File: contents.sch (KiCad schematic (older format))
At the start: 38 parts

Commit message: power
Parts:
- removed C?: 22u, Discret:C1V8, symbol CP
- removed C?: 1u, Capacitors_SMD:C_1210_HandSoldering, symbol C
- removed C?: 0,47u, Capacitors_SMD:C_1210_HandSoldering, symbol C
- removed U?: 7805, TO_SOT_Packages_THT:TO-220_Neutral123_Horizontal, symbol 7805
- added C?: 470uF, symbol CP
- added C?: 10uF, symbol C
- added C?: 100nF, symbol C
- added D?: D_Schottky, symbol D_Schottky
- added P?: Power jack, Pin_Headers:Pin_Header_Straight_1x02, symbol CONN_01X02
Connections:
- wire segments 83 -> 90
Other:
- moved on the sheet: U?
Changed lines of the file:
@@
-$EndComp
-$Comp
-L +12V #PWR?
-U 1 1 595CD701
-P 2200 5500
-F 0 "#PWR?" H 2200 5350 50  0001 C CNN
-F 1 "+12V" H 2200 5640 50  0000 C CNN
-F 2 "" H 2200 5500 50  0000 C CNN
-F 3 "" H 2200 5500 50  0000 C CNN
-	1    2200 5500
-	0    -1   -1   0
-$EndComp
-$Comp
-L 7805 U?
-U 1 1 595CD702
-P 3000 5550
-F 0 "U?" H 3150 5354 50  0000 C CNN
-F 1 "7805" H 3000 5750 50  0000 C CNN
-F 2 "TO_SOT_Packages_THT:TO-220_Neutral123_Horizontal" H 3000 5550 50  0001 C CNN
-F 3 "" H 3000 5550 50  0000 C CNN
-	1    3000 5550
-	1    0    0    -1
-$EndComp
-$Comp
-L GND #PWR?
-U 1 1 595CD703
-P 3000 6100
-F 0 "#PWR?" H 3000 5850 50  0001 C CNN
-F 1 "GND" H 3000 5950 50  0000 C CNN
-F 2 "" H 3000 6100 50  0000 C CNN
-F 3 "" H 3000 6100 50  0000 C CNN
-	1    3000 6100
-	1    0    0    -1
-$EndComp
-$Comp
-L CP C?
-U 1 1 595CD704
-P 2300 5650
-F 0 "C?" H 2325 5750 50  0000 L CNN
-F 1 "22u" H 2325 5550 50  0000 L CNN
-F 2 "Discret:C1V8" H 2338 5500 50  0001 C CNN
-F 3 "" H 2300 5650 50  0000 C CNN
-	1    2300 5650
-	1    0    0    -1
-$EndComp
-$Comp
-L C C?
-U 1 1 595CD705
-P 2550 5650
-F 0 "C?" H 2575 5750 50  0000 L CNN
-F 1 "1u" H 2575 5550 50  0000 L CNN
-F 2 "Capacitors_SMD:C_1210_HandSoldering" H 2588 5500 50  0001 C CNN
-F 3 "" H 2550 5650 50  0000 C CNN
-	1    2550 5650
-	1    0    0    -1
-$EndComp
-$Comp
-L C C?
-U 1 1 595CD706
-P 3800 5650
-F 0 "C?" H 3825 5750 50  0000 L CNN
-F 1 "0,47u" H 3825 5550 50  0000 L CNN
-F 2 "Capacitors_SMD:C_1210_HandSoldering" H 3838 5500 50  0001 C CNN
-F 3 "" H 3800 5650 50  0000 C CNN
-	1    3800 5650
-	1    0    0    -1
-$EndComp
-$Comp
-L +5V #PWR?
-U 1 1 595CD707
-P 4300 5500
-F 0 "#PWR?" H 4300 5350 50  0001 C CNN
-F 1 "+5V" H 4300 5640 50  0000 C CNN
-F 2 "" H 4300 5500 50  0000 C CNN
-F 3 "" H 4300 5500 50  0000 C CNN
-	1    4300 5500
-	0    1    1    0
-$EndComp
-$Comp
-L GND #PWR?
-U 1 1 595CD708
-P 2450 6100
-F 0 "#PWR?" H 2450 5850 50  0001 C CNN
-F 1 "GND" H 2450 5950 50  0000 C CNN
-F 2 "" H 2450 6100 50  0000 C CNN
-F 3 "" H 2450 6100 50  0000 C CNN
-	1    2450 6100
-	1    0    0    -1
-$EndComp
-$Comp
-L GND #PWR?
-U 1 1 595CD709
-P 3800 6100
-F 0 "#PWR?" H 3800 5850 50  0001 C CNN
-F 1 "GND" H 3800 5950 50  0000 C CNN
-F 2 "" H 3800 6100 50  0000 C CNN
-F 3 "" H 3800 6100 50  0000 C CNN
-	1    3800 6100
-	1    0    0    -1
 $EndComp
 $Comp
@@
 L GND #PWR?
 U 1 1 595CD70B
-P 1500 5800
-F 0 "#PWR?" H 1500 5550 50  0001 C CNN
-F 1 "GND" H 1500 5650 50  0000 C CNN
-F 2 "" H 1500 5800 50  0000 C CNN
-F 3 "" H 1500 5800 50  0000 C CNN
-	1    1500 5800
+P 1500 6100
+F 0 "#PWR?" H 1500 5850 50  0001 C CNN
+F 1 "GND" H 1500 5950 50  0000 C CNN
+F 2 "" H 1500 6100 50  0000 C CNN
+F 3 "" H 1500 6100 50  0000 C CNN
+	1    1500 6100
 	1    0    0    -1
 $EndComp
@@
 Connection ~ 10550 5200
 Wire Wire Line
-	2200 5500 2600 5500
-Connection ~ 2300 5500
-Connection ~ 2550 5500
-Wire Wire Line
-	2300 5800 2550 5800
-Wire Wire Line
-	2450 6100 2450 5800
-Connection ~ 2450 5800
-Wire Wire Line
-	3000 5800 3000 6100
-Wire Wire Line
-	3400 5500 4300 5500
-Connection ~ 3800 5500
-Wire Wire Line
-	3800 5800 3800 6100
-Wire Wire Line
-	1300 5500 1550 5500
+	1300 5500 1750 5500
 Wire Wire Line
 	1300 5600 1500 5600
 Wire Wire Line
-	1500 5600 1500 5800
+	1500 5600 1500 6100
 $Comp
 L POT-RESCUE-Arpette RV?
@@
 Wire Wire Line
 	10550 5550 8500 5550
-Entry Wire Line
-	1200 5500 1300 5600
 Text GLabel 8850 1750 0    60   Input ~ 0
 SSR3
@@
 L TPS54302 U?
 U 1 1 59A7BEB1
-P 3000 4850
-F 0 "U?" H 3000 4650 60  0000 C CNN
-F 1 "TPS54302" H 3000 4850 60  0000 C CNN
-F 2 "" H 3100 4850 60  0001 C CNN
-F 3 "" H 3100 4850 60  0001 C CNN
-	1    3000 4850
-	1    0    0    -1
-$EndComp
+P 4350 5700
+F 0 "U?" H 4350 5500 60  0000 C CNN
+F 1 "TPS54302" H 4350 5700 60  0000 C CNN
+F 2 "" H 4450 5700 60  0001 C CNN
+F 3 "" H 4450 5700 60  0001 C CNN
+	1    4350 5700
+	1    0    0    -1
+$EndComp
+$Comp
+L D_Schottky D?
+U 1 1 59A80FF7
+P 1900 5500
+F 0 "D?" H 1900 5600 50  0000 C CNN
+F 1 "D_Schottky" H 1900 5400 50  0000 C CNN
+F 2 "" H 1900 5500 50  0001 C CNN
+F 3 "" H 1900 5500 50  0001 C CNN
+	1    1900 5500
+	-1   0    0    1
+$EndComp
+$Comp
+L CONN_01X02 P?
+U 1 1 59A81E1F
+P 1100 4950
+F 0 "P?" H 1100 5100 50  0000 C CNN
+F 1 "Power jack" V 1200 4950 50  0000 C CNN
+F 2 "Pin_Headers:Pin_Header_Straight_1x02" H 1100 4950 50  0001 C CNN
+F 3 "" H 1100 4950 50  0000 C CNN
+	1    1100 4950
+	-1   0    0    1
+$EndComp
+$Comp
+L GND #PWR?
+U 1 1 59A81F07
+P 1500 5150
+F 0 "#PWR?" H 1500 4900 50  0001 C CNN
+F 1 "GND" H 1500 5000 50  0000 C CNN
+F 2 "" H 1500 5150 50  0000 C CNN
+F 3 "" H 1500 5150 50  0000 C CNN
+	1    1500 5150
+	1    0    0    -1
+$EndComp
+Wire Wire Line
+	1300 5000 1500 5000
+Wire Wire Line
+	1500 5000 1500 5150
+Wire Wire Line
+	1650 5500 1650 4900
+Wire Wire Line
+	1650 4900 1300 4900
+Connection ~ 1650 5500
+$Comp
+L CP C?
+U 1 1 59A94127
+P 2150 5750
+F 0 "C?" H 2175 5850 50  0000 L CNN
+F 1 "470uF" H 2175 5650 50  0000 L CNN
+F 2 "" H 2188 5600 50  0001 C CNN
+F 3 "" H 2150 5750 50  0001 C CNN
+	1    2150 5750
+	1    0    0    -1
+$EndComp
+$Comp
+L C C?
+U 1 1 59A94628
+P 2450 5750
+F 0 "C?" H 2475 5850 50  0000 L CNN
+F 1 "10uF" H 2475 5650 50  0000 L CNN
+F 2 "" H 2488 5600 50  0001 C CNN
+F 3 "" H 2450 5750 50  0001 C CNN
+	1    2450 5750
+	1    0    0    -1
+$EndComp
+Wire Wire Line
+	2050 5500 3700 5500
+Wire Wire Line
+	2150 5500 2150 5600
+Wire Wire Line
+	2450 5500 2450 5600
+Connection ~ 2150 5500
+Connection ~ 2450 5500
+$Comp
+L C C?
+U 1 1 59A94B39
+P 2800 5750
+F 0 "C?" H 2825 5850 50  0000 L CNN
+F 1 "100nF" H 2825 5650 50  0000 L CNN
+F 2 "" H 2838 5600 50  0001 C CNN
+F 3 "" H 2800 5750 50  0001 C CNN
+	1    2800 5750
+	1    0    0    -1
+$EndComp
+$Comp
+L GND #PWR?
+U 1 1 59A963C8
+P 2150 6100
+F 0 "#PWR?" H 2150 5850 50  0001 C CNN
+F 1 "GND" H 2150 5950 50  0000 C CNN
+F 2 "" H 2150 6100 50  0000 C CNN
+F 3 "" H 2150 6100 50  0000 C CNN
+	1    2150 6100
+	1    0    0    -1
+$EndComp
+$Comp
+L GND #PWR?
+U 1 1 59A96448
+P 2450 6100
+F 0 "#PWR?" H 2450 5850 50  0001 C CNN
+F 1 "GND" H 2450 5950 50  0000 C CNN
+F 2 "" H 2450 6100 50  0000 C CNN
+F 3 "" H 2450 6100 50  0000 C CNN
+	1    2450 6100
+	1    0    0    -1
+$EndComp
+$Comp
+L GND #PWR?
+U 1 1 59A964C8
+P 2800 6100
+F 0 "#PWR?" H 2800 5850 50  0001 C CNN
+F 1 "GND" H 2800 5950 50  0000 C CNN
+F 2 "" H 2800 6100 50  0000 C CNN
+F 3 "" H 2800 6100 50  0000 C CNN
+	1    2800 6100
+	1    0    0    -1
+$EndComp
+Wire Wire Line
+	2150 5900 2150 6100
+Wire Wire Line
+	2450 5900 2450 6100
+Wire Wire Line
+	2800 5900 2800 6100
+Wire Wire Line
+	2800 5600 2800 5500
+Connection ~ 2800 5500
+$Comp
+L GND #PWR?
+U 1 1 59A96903
+P 3450 5750
+F 0 "#PWR?" H 3450 5500 50  0001 C CNN
+F 1 "GND" H 3450 5600 50  0000 C CNN
+F 2 "" H 3450 5750 50  0000 C CNN
+F 3 "" H 3450 5750 50  0000 C CNN
+	1    3450 5750
+	1    0    0    -1
+$EndComp
+Wire Wire Line
+	3450 5750 3450 5700
+Wire Wire Line
+	3450 5700 3700 5700
 $EndSCHEMATC

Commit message: Power supply
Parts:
- added C?: 100nF, symbol C
- added C? (x2): 22uF, symbol C
- added C?: 75pF, symbol C
- added C?: 470uF, symbol CP
- added L?: L_Core_Ferrite, symbol L_Core_Ferrite
- added R?: 511k, symbol R
- added R?: 105k, symbol R
- added R?: 49.9, symbol R
- added R?: 100k, symbol R
- added R?: 13.3k, symbol R
- added U?: LF50_TO220, TO_SOT_Packages_THT:TO-220_Vertical, symbol LF50_TO220
- U?: value TL971 -> LM321
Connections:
- net labels added: +VDC, 5V
- net labels removed: +12V
- wire segments 90 -> 117
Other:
- moved on the sheet: C?, D?, P?, Q?, R?, RV?, U?

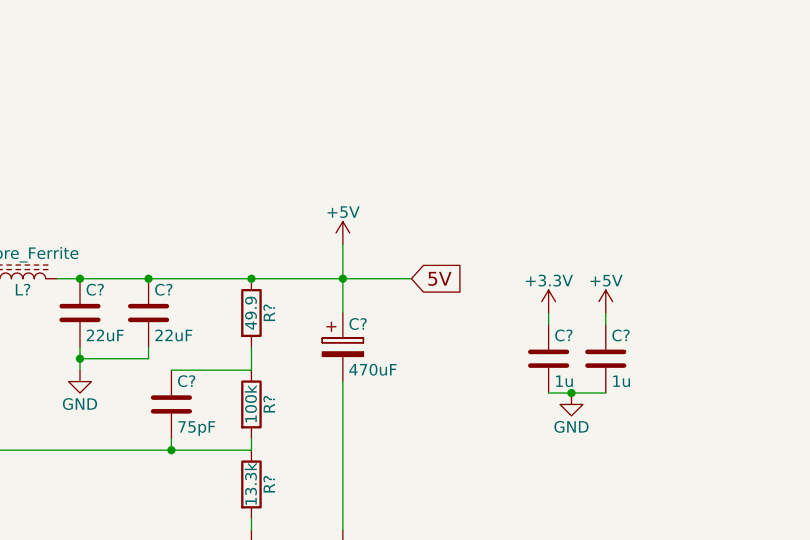
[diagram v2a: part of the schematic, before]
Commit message: Added multiple inputs
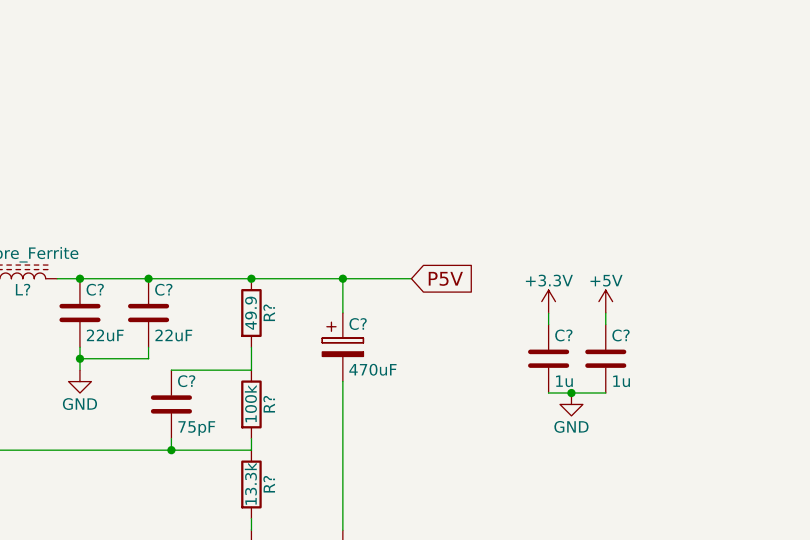
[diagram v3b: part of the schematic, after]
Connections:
- net labels added: P5V
- net labels removed: 5V
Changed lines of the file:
@@
 $EndComp
 Text GLabel 8450 1250 2    60   Input ~ 0
-5V
+P5V
 $Comp
 L +VDC #PWR?
@@
 $EndComp
 $Comp
-L +5V #PWR?
-U 1 1 59AF6636
-P 8150 1100
-F 0 "#PWR?" H 8150 950 50  0001 C CNN
-F 1 "+5V" H 8150 1240 50  0000 C CNN
-F 2 "" H 8150 1100 50  0001 C CNN
-F 3 "" H 8150 1100 50  0001 C CNN
-	1    8150 1100
-	1    0    0    -1
-$EndComp
-$Comp
 L CP C?
 U 1 1 59AF66DA
@@
 Wire Wire Line
 	1550 700  1700 700
-Wire Wire Line
-	8150 1100 8150 1400
-Connection ~ 8150 1250
 $Comp
 L GND #PWR?
@@
 Wire Wire Line
 	2800 1650 2450 1650
+Wire Wire Line
+	8150 1400 8150 1250
+Connection ~ 8150 1250
 $EndSCHEMATC

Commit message: LDO
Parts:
- added C?: 470uF, low ESR, symbol CP
- added C?: 47uF, low ESR, symbol CP
- U?: value LF50_TO220 -> LM3940_SOT223; symbol LF50_TO220 -> SPX2920M3-3.3
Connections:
- wire segments 117 -> 122
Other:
- note added: "Linear LDO regulator 5V ->3.3V, 1A"
- note added: "SMPS 9-28V -> 5V, 3A"
- moved on the sheet: C?, D?, L?, P?, R?, U?

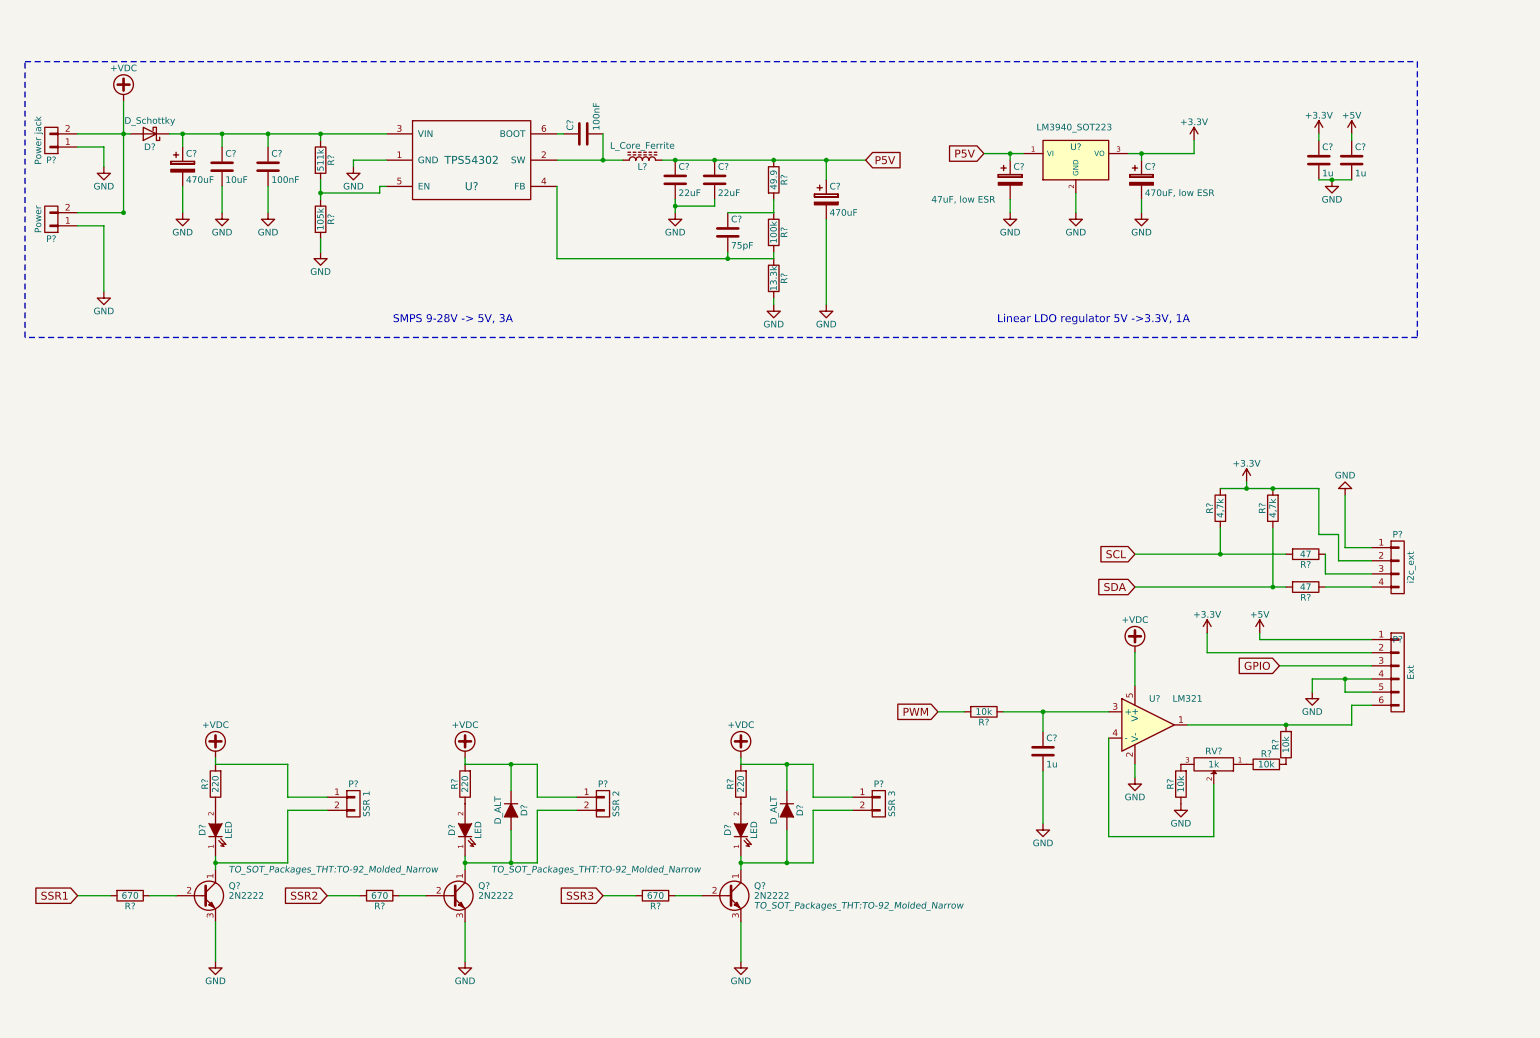
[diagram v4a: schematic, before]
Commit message: Peripherals added
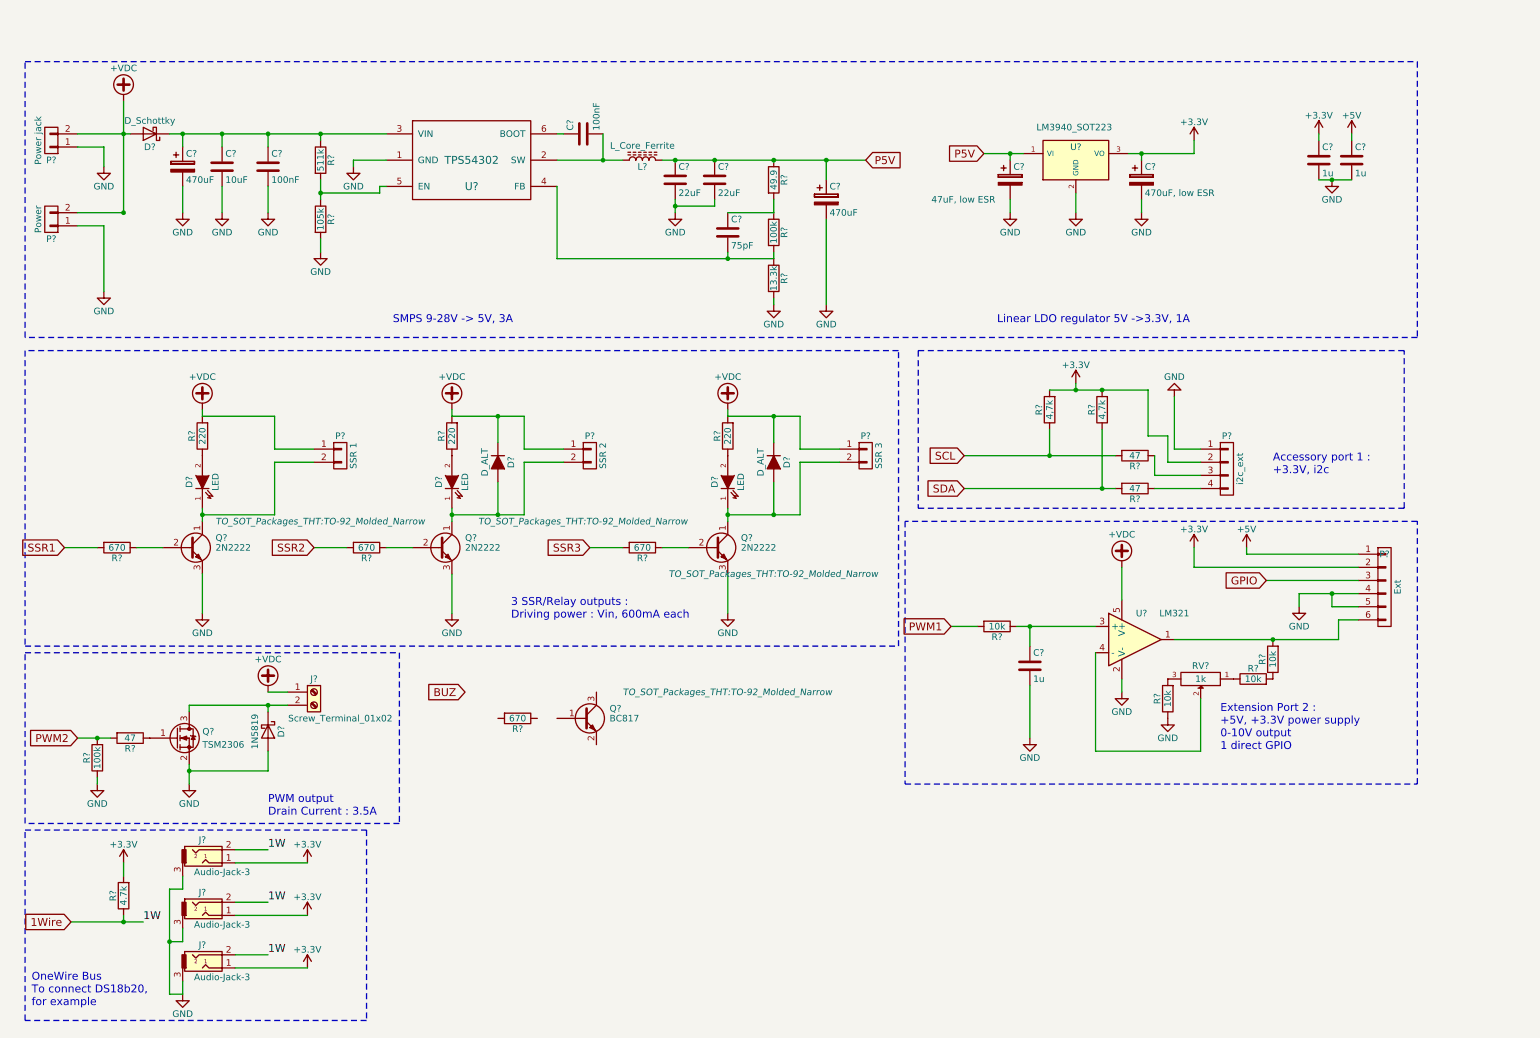
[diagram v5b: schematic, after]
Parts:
- added D?: 1N5819, symbol D_Schottky
- added J?: Screw_Terminal_01x02, symbol Screw_Terminal_01x02
- added J? (x3): Audio-Jack-3, symbol Audio-Jack-3
- added Q?: TSM2306, symbol Q_NMOS_GSD
- added Q?: BC817, TO_SOT_Packages_THT:TO-92_Molded_Narrow, symbol BC817
- added R?: 47, Resistors_ThroughHole:Resistor_Horizontal_RM10mm, symbol R
- added R?: 100k, Resistors_ThroughHole:Resistor_Horizontal_RM10mm, symbol R
- added R?: 4.7k, Resistors_ThroughHole:Resistor_Horizontal_RM10mm, symbol R
- added R?: 670, Resistors_ThroughHole:Resistor_Horizontal_RM10mm, symbol R
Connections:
- net +3V3: now also J?.1, J?.1, J?.1, R?.2
- net +VDC: now also J?.1 (Pin_1)
- net GND: now also D?.2 (A), J?.3, J?.3, J?.3, Q?.2 (S), R?.1
- net PWM renamed PWM1
- new net: Q?.1 (G), R?.1
- new net: D?.1 (K), J?.2 (Pin_2), Q?.3 (D)
- new net 1Wire: J?.2, J?.2, J?.2, R?.1
- new net PWM2: R?.2, R?.2
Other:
- note added: "3 SSR/Relay outputs :\nDriving power : Vin, 600mA each"
- note added: "Accessory port 1 :\n+3.3V, i2c"
- note added: "Extension Port 2 :\n+5V, +3.3V power supply\n0-10V output\n1 direct GPIO"
- note added: "OneWire Bus\nTo connect DS18b20,\nfor example"
- note added: "PWM output\nDrain Current : 3.5A"
- moved on the sheet: C?, D?, P?, Q?, R?, RV?, U?
